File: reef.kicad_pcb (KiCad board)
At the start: 2 copper layers, 85 parts, among them J1 Conn_01x05_Female, J2 Conn_01x02_Male, U1 nice_nano, U2 TRRS, U3 TRRS

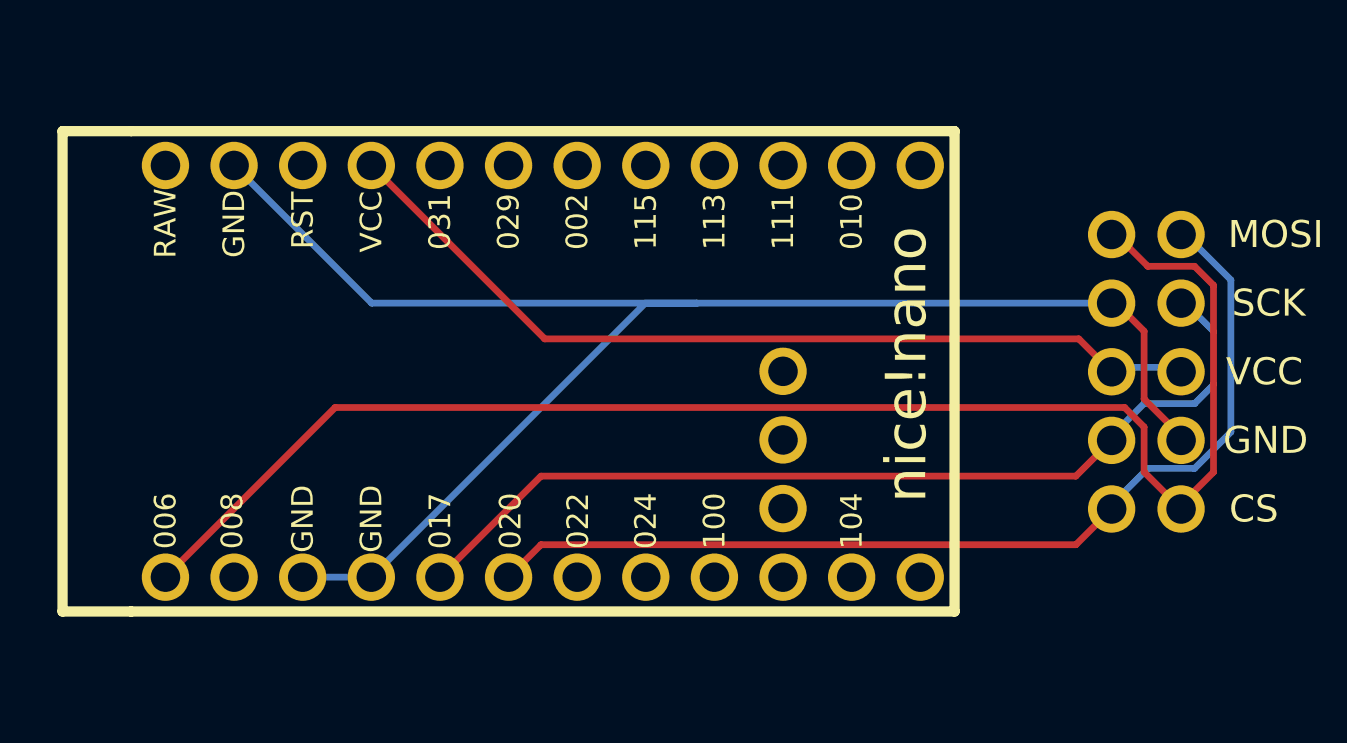
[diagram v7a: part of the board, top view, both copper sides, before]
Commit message: new submodule for reversible footprints
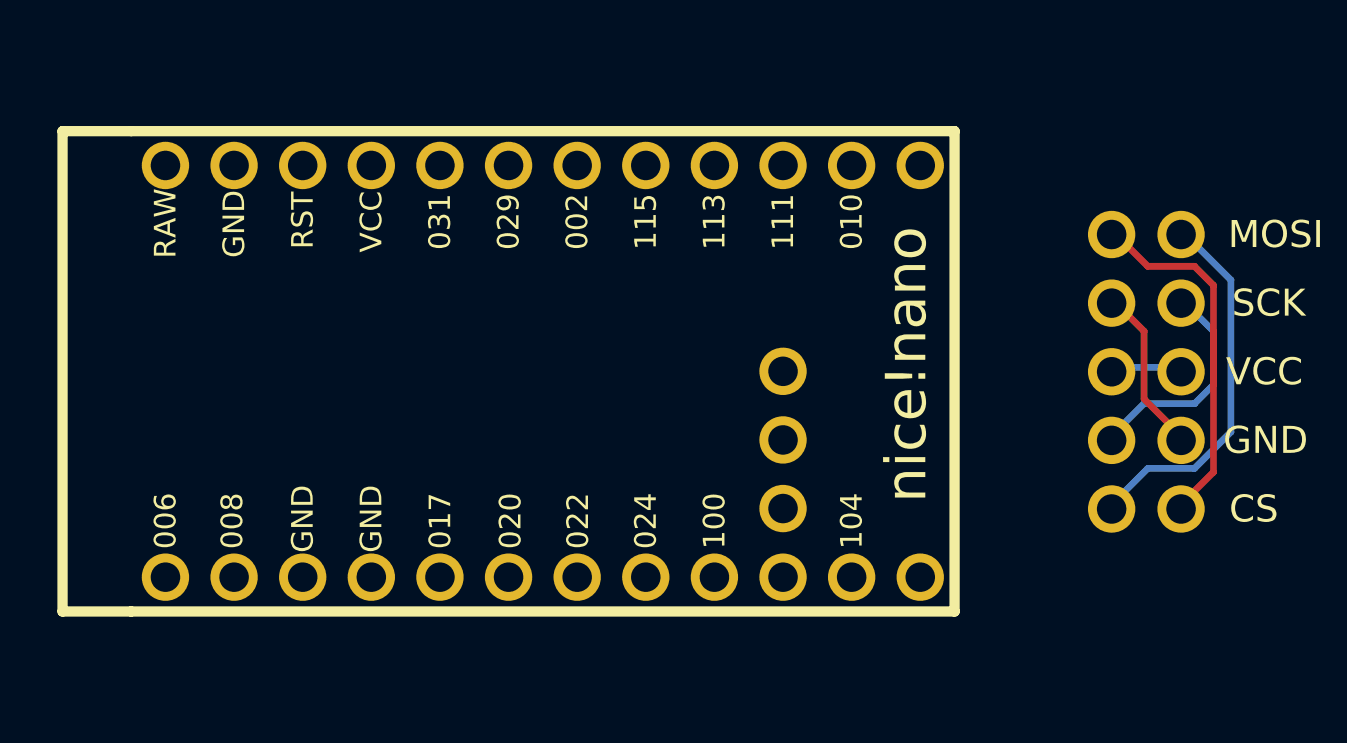
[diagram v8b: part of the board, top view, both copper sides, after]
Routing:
- net gnd: track 62.8 -> 9.38 mm
- net cs: track 56.0 -> 13.2 mm
- net vcc: track 33.1 -> 2.57 mm
- net sck: track 35.2 -> 8.24 mm
- net mosi: track 37.1 -> 13.8 mm
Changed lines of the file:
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@@
   (segment (start 115.94625 100.568341) (end 119.359159 103.98125) (width 0.25) (layer "B.Cu") (net 43))
   (segment (start 119.359159 103.98125) (end 123.03125 103.98125) (width 0.25) (layer "B.Cu") (net 43))
-  (segment (start 164.987297 43.725439) (end 145.187061 43.725439) (width 0.25) (layer "F.Cu") (net 47))
-  (segment (start 145.187061 43.725439) (end 143.98625 44.92625) (width 0.25) (layer "F.Cu") (net 47))
-  (segment (start 166.310439 42.402297) (end 164.987297 43.725439) (width 0.25) (layer "F.Cu") (net 47))
   (segment (start 170.725439 39.553204) (end 170.725439 33.925) (width 0.25) (layer "B.Cu") (net 47))
   (segment (start 166.310439 42.24) (end 167.649628 40.900811) (width 0.25) (layer "B.Cu") (net 47))
@@
   (segment (start 169.377832 40.900811) (end 170.725439 39.553204) (width 0.25) (layer "B.Cu") (net 47))
   (segment (start 167.649628 40.900811) (end 169.377832 40.900811) (width 0.25) (layer "B.Cu") (net 47))
-  (segment (start 145.187061 41.185439) (end 164.987297 41.185439) (width 0.25) (layer "F.Cu") (net 48))
-  (segment (start 164.987297 41.185439) (end 166.310439 39.862297) (width 0.25) (layer "F.Cu") (net 48))
-  (segment (start 141.44625 44.92625) (end 145.187061 41.185439) (width 0.25) (layer "F.Cu") (net 48))
   (segment (start 168.880439 34.62) (end 170.08125 35.820811) (width 0.25) (layer "B.Cu") (net 48))
   (segment (start 167.51125 38.499189) (end 166.310439 39.7) (width 0.25) (layer "B.Cu") (net 48))
@@
   (segment (start 170.08125 35.820811) (end 170.08125 37.804189) (width 0.25) (layer "B.Cu") (net 48))
   (segment (start 170.08125 37.804189) (end 169.38625 38.499189) (width 0.25) (layer "B.Cu") (net 48))
-  (segment (start 166.310439 37.322297) (end 165.093581 36.105439) (width 0.25) (layer "F.Cu") (net 50))
-  (segment (start 145.325439 36.105439) (end 138.90625 29.68625) (width 0.25) (layer "F.Cu") (net 50))
-  (segment (start 165.093581 36.105439) (end 145.325439 36.105439) (width 0.25) (layer "F.Cu") (net 50))
   (segment (start 168.880439 37.16) (end 166.310439 37.16) (width 0.25) (layer "B.Cu") (net 50))
   (segment (start 167.51125 35.820811) (end 166.310439 34.62) (width 0.25) (layer "F.Cu") (net 53))
   (segment (start 167.51125 38.330811) (end 167.51125 35.820811) (width 0.25) (layer "F.Cu") (net 53))
   (segment (start 168.880439 39.7) (end 167.51125 38.330811) (width 0.25) (layer "F.Cu") (net 53))
-  (segment (start 150.955203 34.782297) (end 138.922297 34.782297) (width 0.25) (layer "B.Cu") (net 53))
-  (segment (start 149.050203 34.782297) (end 150.955203 34.782297) (width 0.25) (layer "B.Cu") (net 53))
-  (segment (start 138.90625 44.92625) (end 149.050203 34.782297) (width 0.25) (layer "B.Cu") (net 53))
   (segment (start 74.602125 33.0335) (end 77.842125 33.0335) (width 0.25) (layer "B.Cu") (net 53))
-  (segment (start 136.36625 44.92625) (end 138.90625 44.92625) (width 0.25) (layer "B.Cu") (net 53))
-  (segment (start 138.922297 34.782297) (end 133.82625 29.68625) (width 0.25) (layer "B.Cu") (net 53))
-  (segment (start 166.310439 34.782297) (end 150.955203 34.782297) (width 0.25) (layer "B.Cu") (net 53))
-  (segment (start 167.51125 39.364904) (end 166.791785 38.645439) (width 0.25) (layer "F.Cu") (net 54))
   (segment (start 170.08125 41.039189) (end 170.08125 34.122607) (width 0.25) (layer "F.Cu") (net 54))
-  (segment (start 168.880439 42.402297) (end 167.51125 41.033108) (width 0.25) (layer "F.Cu") (net 54))
   (segment (start 168.880439 42.24) (end 170.08125 41.039189) (width 0.25) (layer "F.Cu") (net 54))
-  (segment (start 166.791785 38.645439) (end 137.567061 38.645439) (width 0.25) (layer "F.Cu") (net 54))
-  (segment (start 137.567061 38.645439) (end 131.28625 44.92625) (width 0.25) (layer "F.Cu") (net 54))
   (segment (start 167.649628 33.419189) (end 166.310439 32.08) (width 0.25) (layer "F.Cu") (net 54))
   (segment (start 169.377832 33.419189) (end 167.649628 33.419189) (width 0.25) (layer "F.Cu") (net 54))
-  (segment (start 167.51125 41.033108) (end 167.51125 39.364904) (width 0.25) (layer "F.Cu") (net 54))
   (segment (start 170.08125 34.122607) (end 169.377832 33.419189) (width 0.25) (layer "F.Cu") (net 54))
   (segment (start 72.602125 32.56975) (end 74.215625 30.95625) (width 0.25) (layer "B.Cu") (net 55))
@@
     )
   )
-  (group "" (id 761bdc9b-636f-4803-9a81-12b66696b9d7)
-    (members
-      00dc3ea5-81b5-4281-ab77-0b69fbfc10ec
-      00f572fa-8cf5-4237-a82d-629cad713cc6
-      099b2216-8e3c-40ee-9b4a-9ff228af64c0
-      169dfd57-b411-4d8d-8ea4-0e4f07b3ae8c
-      16f1451c-e720-40ce-b177-6bfe9aa1c209
-      1e3a58d6-5283-4b20-a5ff-a95dfe01f76c
-      207a3cb6-c23d-422f-9c44-5ef803db747c
-      22112936-a565-47d3-aec3-99f6a74a9b4a
-      2534f191-f7df-4ce7-bffb-c921eef51fd0
-      29f74d31-a44a-4564-b511-192395990d5f
-      2f1f222f-02f5-411a-a7e7-f690797fbe53
-      33006d50-9a38-484a-9919-a16fd722e7a5
-      37e91b2e-8f36-40fc-9961-24cdc0cf0c14
-      3a25df0b-7d30-420c-a33d-cc8995332ef6
-      4a26203e-fcf0-4e21-8d6e-9ea80221c900
-      51e793c8-0bc7-458b-aeeb-7ae4e914fcd5
-      544e5c38-dcb0-46c2-9307-024100a05ce0
-      5e8500a9-e36e-49ef-9bb7-8d118d43124c
-      6ca3cf70-24ce-4d43-8d11-c74a32fde5cd
-      6d0cbd15-8b3c-4581-bde4-b57056823994
-      732ffaad-9fd6-4564-9397-575e758f54c0
-      761c8e29-382a-475c-a37a-7201cc9cd0f5
-      763e73b4-dbeb-4c22-a598-4a2eea19b308
-      76ac3dd0-d9da-4015-9fff-c0968a3153d4
-      78ee076b-8fff-4dc0-89d8-eb4542d0a929
-      79c511ff-941d-47d4-85f4-51b7208629ba
-      8c6588a3-b4ea-428f-bade-59f12759db05
-      92d86137-2e43-4679-ae0e-02c0144eae2d
-      9495b690-59a2-40cd-854c-24bdd9ac2f48
-      bb4b00e4-0ebb-464e-bff0-03db85270523
-      c486bc9c-74d9-44e6-9b10-7eea73aebd0e
-      ca0bab8d-c1a4-4932-98c0-1f35f3008bf8
-      cc920e06-0927-43b6-a842-1c5c661e0f38
-      cfaac7ac-0d9f-4c8a-9c58-4c0672af1e66
-      d4b4a14a-908c-474c-b46b-41adc3b5848a
-      d5fc7494-b778-4b6b-b23a-7905f04b9019
-      d86ef0a3-2314-47cc-a618-360f238317d7
-      e0143cfc-1ec2-428a-8991-c1bbf7260e17
-      e52e7333-6811-48c1-b1a8-3dad748c2672
-      e741eb38-339e-46bf-98f9-cd52b4510dda
-      f2a5304c-b95e-4ebf-8701-0cb8c4f3434c
-      f595db3b-639a-49be-8b49-e445fb2d4eae
-    )
-  )
